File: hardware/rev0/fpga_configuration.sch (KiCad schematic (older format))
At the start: 25 parts, among them IC1 ECP5-BGA256, J5 Conn_ARM_JTAG_SWD_10, J6 Conn_ARM_JTAG_SWD_10, U6 ATSAMD21G18A-AUT, U7 W25Q32JVSS

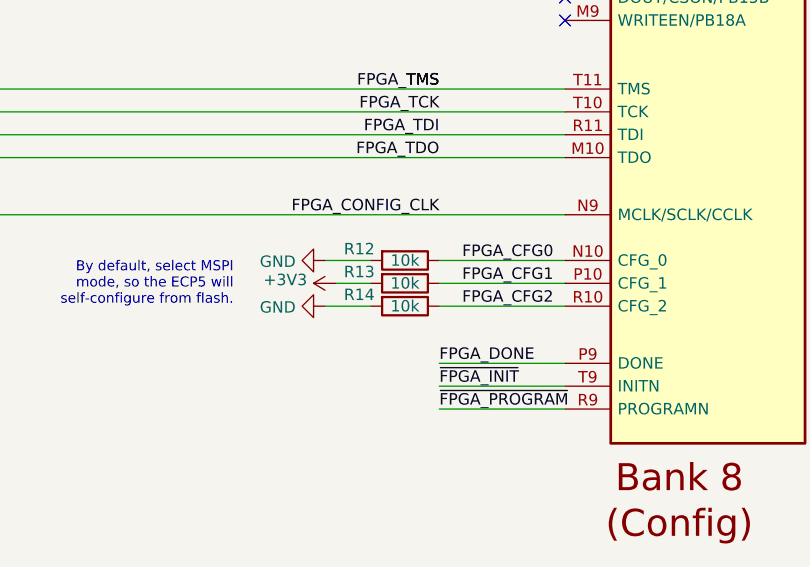
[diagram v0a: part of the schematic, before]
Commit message: hardware: add part numbers
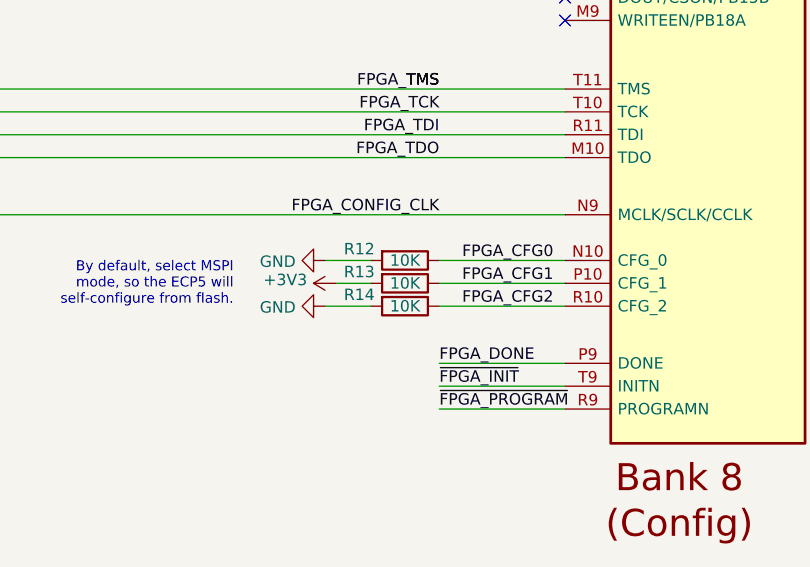
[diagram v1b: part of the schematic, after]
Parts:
- D10, D14: Manufacturer_Part_Number (none) -> GENERIC-LED-0603-BLUE
- D11, D13: Manufacturer_Part_Number (none) -> GENERIC-LED-0603-PINK
- D12: Manufacturer_Part_Number (none) -> GENERIC-LED-0603-WHITE
- J5, J6: Description (none) -> CONN HEADER VERT 10POS 1.27MM; Manufacturer_Name (none) -> Samtec; Manufacturer_Part_Number (none) -> FTSH-105-01-F-D-K
- R10, R11, R7, R8, R9: Manufacturer_Part_Number (none) -> GENERIC-RES-0402-330
- R12, R13, R14: value 10k -> 10K; Manufacturer_Part_Number (none) -> GENERIC-RES-0402-10K
- R25: Manufacturer_Part_Number (none) -> GENERIC-RES-0402-10K
- U6: Description (none) -> IC MCU 32BIT 256KB FLASH 48TQFP; Manufacturer_Name (none) -> Microchip; Manufacturer_Part_Number (none) -> ATSAMD21G18A-AUT
- U7: Description (none) -> IC FLASH 32M SPI 133MHZ 8SOIC; Manufacturer_Name (none) -> Winbond; Manufacturer_Part_Number (none) -> W25Q32JVSSIQ
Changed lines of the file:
@@
 EESchema Schematic File Version 4
-LIBS:luna_rev0-cache
 EELAYER 30 0
 EELAYER END
@@
 F 2 "Package_SO:SOIC-8_5.23x5.23mm_P1.27mm" H 7850 1350 50  0001 C CNN
 F 3 "http://www.winbond.com/resource-files/w25q32jv%20revg%2003272018%20plus.pdf" H 7850 1350 50  0001 C CNN
+F 4 "IC FLASH 32M SPI 133MHZ 8SOIC" H 7850 1350 50  0001 C CNN "Description"
+F 5 "Winbond" H 7850 1350 50  0001 C CNN "Manufacturer_Name"
+F 6 "W25Q32JVSSIQ" H 7850 1350 50  0001 C CNN "Manufacturer_Part_Number"
 	1    7850 1350
 	1    0    0    -1
@@
 P 8750 4950
 F 0 "R12" V 8700 4750 50  0000 C CNN
-F 1 "10k" V 8750 4950 50  0000 C CNN
+F 1 "10K" V 8750 4950 50  0000 C CNN
 F 2 "Resistor_SMD:R_0402_1005Metric" V 8680 4950 50  0001 C CNN
 F 3 "~" H 8750 4950 50  0001 C CNN
+F 4 "GENERIC-RES-0402-10K" H 8750 4950 50  0001 C CNN "Manufacturer_Part_Number"
 	1    8750 4950
 	0    1    1    0
@@
 P 8750 5050
 F 0 "R13" V 8700 4850 50  0000 C CNN
-F 1 "10k" V 8750 5050 50  0000 C CNN
+F 1 "10K" V 8750 5050 50  0000 C CNN
 F 2 "Resistor_SMD:R_0402_1005Metric" V 8680 5050 50  0001 C CNN
 F 3 "~" H 8750 5050 50  0001 C CNN
+F 4 "GENERIC-RES-0402-10K" H 8750 5050 50  0001 C CNN "Manufacturer_Part_Number"
 	1    8750 5050
 	0    1    1    0
@@
 P 8750 5150
 F 0 "R14" V 8700 4950 50  0000 C CNN
-F 1 "10k" V 8750 5150 50  0000 C CNN
+F 1 "10K" V 8750 5150 50  0000 C CNN
 F 2 "Resistor_SMD:R_0402_1005Metric" V 8680 5150 50  0001 C CNN
 F 3 "~" H 8750 5150 50  0001 C CNN
+F 4 "GENERIC-RES-0402-10K" H 8750 5150 50  0001 C CNN "Manufacturer_Part_Number"
 	1    8750 5150
 	0    1    1    0
@@
 F 2 "luna:SWD_CONNECTOR_LARGE_BOX" H 5850 6650 50  0001 C CNN
 F 3 "http://infocenter.arm.com/help/topic/com.arm.doc.ddi0314h/DDI0314H_coresight_components_trm.pdf" V 5500 5400 50  0001 C CNN
+F 4 "CONN HEADER VERT 10POS 1.27MM" H 5850 6650 50  0001 C CNN "Description"
+F 5 "Samtec" H 5850 6650 50  0001 C CNN "Manufacturer_Name"
+F 6 "FTSH-105-01-F-D-K" H 5850 6650 50  0001 C CNN "Manufacturer_Part_Number"
 	1    5850 6650
 	-1   0    0    -1
@@
 F 2 "LED_SMD:LED_0603_1608Metric_Pad1.05x0.95mm_HandSolder" H 4350 4050 50  0001 C CNN
 F 3 "~" H 4350 4050 50  0001 C CNN
+F 4 "GENERIC-LED-0603-PINK" H 4350 4050 50  0001 C CNN "Manufacturer_Part_Number"
 	1    4350 4050
 	1    0    0    1
@@
 F 2 "LED_SMD:LED_0603_1608Metric_Pad1.05x0.95mm_HandSolder" H 4350 4150 50  0001 C CNN
 F 3 "~" H 4350 4150 50  0001 C CNN
+F 4 "GENERIC-LED-0603-WHITE" H 4350 4150 50  0001 C CNN "Manufacturer_Part_Number"
 	1    4350 4150
 	1    0    0    1
@@
 F 2 "LED_SMD:LED_0603_1608Metric_Pad1.05x0.95mm_HandSolder" H 4350 4250 50  0001 C CNN
 F 3 "~" H 4350 4250 50  0001 C CNN
+F 4 "GENERIC-LED-0603-PINK" H 4350 4250 50  0001 C CNN "Manufacturer_Part_Number"
 	1    4350 4250
 	1    0    0    1
@@
 F 2 "LED_SMD:LED_0603_1608Metric_Pad1.05x0.95mm_HandSolder" H 4350 4350 50  0001 C CNN
 F 3 "~" H 4350 4350 50  0001 C CNN
+F 4 "GENERIC-LED-0603-BLUE" H 4350 4350 50  0001 C CNN "Manufacturer_Part_Number"
 	1    4350 4350
 	1    0    0    1
@@
 F 2 "Resistor_SMD:R_0402_1005Metric" V 3730 3950 50  0001 C CNN
 F 3 "~" H 3800 3950 50  0001 C CNN
+F 4 "GENERIC-RES-0402-330" H 3800 3950 50  0001 C CNN "Manufacturer_Part_Number"
 	1    3800 3950
 	0    1    1    0
@@
 F 2 "Resistor_SMD:R_0402_1005Metric" V 3730 4050 50  0001 C CNN
 F 3 "~" H 3800 4050 50  0001 C CNN
+F 4 "GENERIC-RES-0402-330" H 3800 4050 50  0001 C CNN "Manufacturer_Part_Number"
 	1    3800 4050
 	0    1    1    0
@@
 F 2 "Resistor_SMD:R_0402_1005Metric" V 3730 4150 50  0001 C CNN
 F 3 "~" H 3800 4150 50  0001 C CNN
+F 4 "GENERIC-RES-0402-330" H 3800 4150 50  0001 C CNN "Manufacturer_Part_Number"
 	1    3800 4150
 	0    1    1    0
@@
 F 2 "Resistor_SMD:R_0402_1005Metric" V 3730 4250 50  0001 C CNN
 F 3 "~" H 3800 4250 50  0001 C CNN
+F 4 "GENERIC-RES-0402-330" H 3800 4250 50  0001 C CNN "Manufacturer_Part_Number"
 	1    3800 4250
 	0    1    1    0
@@
 F 2 "Resistor_SMD:R_0402_1005Metric" V 3730 4350 50  0001 C CNN
 F 3 "~" H 3800 4350 50  0001 C CNN
+F 4 "GENERIC-RES-0402-330" H 3800 4350 50  0001 C CNN "Manufacturer_Part_Number"
 	1    3800 4350
 	0    1    1    0
@@
 F 2 "luna:SWD_CONNECTOR_LARGE_BOX" H 1750 6650 50  0001 C CNN
 F 3 "http://infocenter.arm.com/help/topic/com.arm.doc.ddi0314h/DDI0314H_coresight_components_trm.pdf" V 1400 5400 50  0001 C CNN
+F 4 "CONN HEADER VERT 10POS 1.27MM" H 1750 6650 50  0001 C CNN "Description"
+F 5 "Samtec" H 1750 6650 50  0001 C CNN "Manufacturer_Name"
+F 6 "FTSH-105-01-F-D-K" H 1750 6650 50  0001 C CNN "Manufacturer_Part_Number"
 	1    1750 6650
 	-1   0    0    -1
@@
 F 2 "LED_SMD:LED_0603_1608Metric_Pad1.05x0.95mm_HandSolder" H 4350 3950 50  0001 C CNN
 F 3 "~" H 4350 3950 50  0001 C CNN
+F 4 "GENERIC-LED-0603-BLUE" H 4350 3950 50  0001 C CNN "Manufacturer_Part_Number"
 	1    4350 3950
 	1    0    0    1
@@
 F 2 "Resistor_SMD:R_0402_1005Metric" V 5380 5000 50  0001 C CNN
 F 3 "~" H 5450 5000 50  0001 C CNN
+F 4 "GENERIC-RES-0402-10K" H 5450 5000 50  0001 C CNN "Manufacturer_Part_Number"
 	1    5450 5000
 	1    0    0    -1
@@
 F 2 "Package_QFP:TQFP-48_7x7mm_P0.5mm" H 1600 2000 50  0001 C CNN
 F 3 "http://ww1.microchip.com/downloads/en/DeviceDoc/SAMD21-Family-DataSheet-DS40001882D.pdf" H 2550 4750 50  0001 C CNN
+F 4 "IC MCU 32BIT 256KB FLASH 48TQFP" H 2550 3750 50  0001 C CNN "Description"
+F 5 "Microchip" H 2550 3750 50  0001 C CNN "Manufacturer_Name"
+F 6 "ATSAMD21G18A-AUT" H 2550 3750 50  0001 C CNN "Manufacturer_Part_Number"
 	1    2550 3750
 	-1   0    0    -1

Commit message: hardware: normalize BOM fields
make compatible with kicad-bom-scripts
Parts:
- C31, C32, C33, C34, C35, C51: Part Number (none) -> GENERIC-CAP-0402-0.1uF
- D10, D14: Manufacturer_Part_Number GENERIC-LED-0603-BLUE -> (none); Part Number (none) -> GENERIC-LED-0603-BLUE
- D11, D13: Manufacturer_Part_Number GENERIC-LED-0603-PINK -> (none); Part Number (none) -> GENERIC-LED-0603-PINK
- D12: Manufacturer_Part_Number GENERIC-LED-0603-WHITE -> (none); Part Number (none) -> GENERIC-LED-0603-WHITE
- IC1: Height 1.7 -> (none); Manufacturer (none) -> Lattice; Manufacturer_Name Lattice -> (none); Manufacturer_Part_Number LFE5U-12F-6BG256C -> (none); Mouser Part Number 842-LFE5U12F6BG256C -> (none); Mouser Price/Stock https://www.mouser.com/Search/Refine.aspx?Keyword=842-LFE5U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 -> (none); Part Number (none) -> LFE5U-12F-6BG256C
- J5, J6: Manufacturer (none) -> Samtec; Manufacturer_Name Samtec -> (none); Manufacturer_Part_Number FTSH-105-01-F-D-K -> (none); Part Number (none) -> FTSH-105-01-F-D-K
- R10, R11, R7, R8, R9: Manufacturer_Part_Number GENERIC-RES-0402-330 -> (none); Part Number (none) -> GENERIC-RES-0402-330
- R12, R13, R14, R25: Manufacturer_Part_Number GENERIC-RES-0402-10K -> (none); Part Number (none) -> GENERIC-RES-0402-10K
- U6: Manufacturer (none) -> Microchip; Manufacturer_Name Microchip -> (none); Manufacturer_Part_Number ATSAMD21G18A-AUT -> (none); Part Number (none) -> ATSAMD21G18A-AUT
- U7: Manufacturer (none) -> Winbond; Manufacturer_Name Winbond -> (none); Manufacturer_Part_Number W25Q32JVSSIQ -> (none); Part Number (none) -> W25Q32JVSSIQ
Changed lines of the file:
@@
 F 3 "" H 6850 6650 50  0001 L CNN
 F 4 "FPGA - Field Programmable Gate Array ECP5; 12k LUTs; 1.1V" H 6850 6550 50  0001 L CNN "Description"
-F 5 "1.7" H 6850 6900 50  0001 L CNN "Height"
-F 6 "Lattice" H 6900 7500 50  0001 L CNN "Manufacturer_Name"
-F 7 "LFE5U-12F-6BG256C" H 6900 7400 50  0001 L CNN "Manufacturer_Part_Number"
-F 8 "842-LFE5U12F6BG256C" H 7550 6100 50  0001 L CNN "Mouser Part Number"
-F 9 "https://www.mouser.com/Search/Refine.aspx?Keyword=842-LFE5U12F6BG256C" H 7200 5950 50  0001 L CNN "Mouser Price/Stock"
+F 5 "Lattice" H 6900 7500 50  0001 L CNN "Manufacturer"
+F 6 "LFE5U-12F-6BG256C" H 6900 7400 50  0001 L CNN "Part Number"
 	8    10500 2250
 	-1   0    0    -1
@@
 F 2 "Capacitor_SMD:C_0402_1005Metric" H 1438 1150 50  0001 C CNN
 F 3 "~" H 1400 1300 50  0001 C CNN
+F 4 "GENERIC-CAP-0402-0.1uF" H 1400 1300 50  0001 C CNN "Part Number"
 	1    1400 1300
 	1    0    0    -1
@@
 F 2 "Capacitor_SMD:C_0402_1005Metric" H 1738 1150 50  0001 C CNN
 F 3 "~" H 1700 1300 50  0001 C CNN
+F 4 "GENERIC-CAP-0402-0.1uF" H 1700 1300 50  0001 C CNN "Part Number"
 	1    1700 1300
 	1    0    0    -1
@@
 F 2 "Capacitor_SMD:C_0402_1005Metric" H 2038 1150 50  0001 C CNN
 F 3 "~" H 2000 1300 50  0001 C CNN
+F 4 "GENERIC-CAP-0402-0.1uF" H 2000 1300 50  0001 C CNN "Part Number"
 	1    2000 1300
 	1    0    0    -1
@@
 F 2 "Capacitor_SMD:C_0402_1005Metric" H 1138 1150 50  0001 C CNN
 F 3 "~" H 1100 1300 50  0001 C CNN
+F 4 "GENERIC-CAP-0402-0.1uF" H 1100 1300 50  0001 C CNN "Part Number"
 	1    1100 1300
 	1    0    0    -1
@@
 F 3 "http://www.winbond.com/resource-files/w25q32jv%20revg%2003272018%20plus.pdf" H 7850 1350 50  0001 C CNN
 F 4 "IC FLASH 32M SPI 133MHZ 8SOIC" H 7850 1350 50  0001 C CNN "Description"
-F 5 "Winbond" H 7850 1350 50  0001 C CNN "Manufacturer_Name"
-F 6 "W25Q32JVSSIQ" H 7850 1350 50  0001 C CNN "Manufacturer_Part_Number"
+F 5 "Winbond" H 7850 1350 50  0001 C CNN "Manufacturer"
+F 6 "W25Q32JVSSIQ" H 7850 1350 50  0001 C CNN "Part Number"
 	1    7850 1350
 	1    0    0    -1
@@
 F 2 "Capacitor_SMD:C_0402_1005Metric" H 7138 750 50  0001 C CNN
 F 3 "~" H 7100 900 50  0001 C CNN
+F 4 "GENERIC-CAP-0402-0.1uF" H 7100 900 50  0001 C CNN "Part Number"
 	1    7100 900
 	0    1    1    0
@@
 F 2 "Resistor_SMD:R_0402_1005Metric" V 8680 4950 50  0001 C CNN
 F 3 "~" H 8750 4950 50  0001 C CNN
-F 4 "GENERIC-RES-0402-10K" H 8750 4950 50  0001 C CNN "Manufacturer_Part_Number"
+F 4 "GENERIC-RES-0402-10K" H 8750 4950 50  0001 C CNN "Part Number"
 	1    8750 4950
 	0    1    1    0
@@
 F 2 "Resistor_SMD:R_0402_1005Metric" V 8680 5050 50  0001 C CNN
 F 3 "~" H 8750 5050 50  0001 C CNN
-F 4 "GENERIC-RES-0402-10K" H 8750 5050 50  0001 C CNN "Manufacturer_Part_Number"
+F 4 "GENERIC-RES-0402-10K" H 8750 5050 50  0001 C CNN "Part Number"
 	1    8750 5050
 	0    1    1    0
@@
 F 2 "Resistor_SMD:R_0402_1005Metric" V 8680 5150 50  0001 C CNN
 F 3 "~" H 8750 5150 50  0001 C CNN
-F 4 "GENERIC-RES-0402-10K" H 8750 5150 50  0001 C CNN "Manufacturer_Part_Number"
+F 4 "GENERIC-RES-0402-10K" H 8750 5150 50  0001 C CNN "Part Number"
 	1    8750 5150
 	0    1    1    0
@@
 F 3 "http://infocenter.arm.com/help/topic/com.arm.doc.ddi0314h/DDI0314H_coresight_components_trm.pdf" V 5500 5400 50  0001 C CNN
 F 4 "CONN HEADER VERT 10POS 1.27MM" H 5850 6650 50  0001 C CNN "Description"
-F 5 "Samtec" H 5850 6650 50  0001 C CNN "Manufacturer_Name"
-F 6 "FTSH-105-01-F-D-K" H 5850 6650 50  0001 C CNN "Manufacturer_Part_Number"
+F 5 "Samtec" H 5850 6650 50  0001 C CNN "Manufacturer"
+F 6 "FTSH-105-01-F-D-K" H 5850 6650 50  0001 C CNN "Part Number"
 	1    5850 6650
 	-1   0    0    -1
@@
 F 2 "LED_SMD:LED_0603_1608Metric_Pad1.05x0.95mm_HandSolder" H 4350 4050 50  0001 C CNN
 F 3 "~" H 4350 4050 50  0001 C CNN
-F 4 "GENERIC-LED-0603-PINK" H 4350 4050 50  0001 C CNN "Manufacturer_Part_Number"
+F 4 "GENERIC-LED-0603-PINK" H 4350 4050 50  0001 C CNN "Part Number"
 	1    4350 4050
 	1    0    0    1
@@
 F 2 "LED_SMD:LED_0603_1608Metric_Pad1.05x0.95mm_HandSolder" H 4350 4150 50  0001 C CNN
 F 3 "~" H 4350 4150 50  0001 C CNN
-F 4 "GENERIC-LED-0603-WHITE" H 4350 4150 50  0001 C CNN "Manufacturer_Part_Number"
+F 4 "GENERIC-LED-0603-WHITE" H 4350 4150 50  0001 C CNN "Part Number"
 	1    4350 4150
 	1    0    0    1
@@
 F 2 "LED_SMD:LED_0603_1608Metric_Pad1.05x0.95mm_HandSolder" H 4350 4250 50  0001 C CNN
 F 3 "~" H 4350 4250 50  0001 C CNN
-F 4 "GENERIC-LED-0603-PINK" H 4350 4250 50  0001 C CNN "Manufacturer_Part_Number"
+F 4 "GENERIC-LED-0603-PINK" H 4350 4250 50  0001 C CNN "Part Number"
 	1    4350 4250
 	1    0    0    1
@@
 F 2 "LED_SMD:LED_0603_1608Metric_Pad1.05x0.95mm_HandSolder" H 4350 4350 50  0001 C CNN
 F 3 "~" H 4350 4350 50  0001 C CNN
-F 4 "GENERIC-LED-0603-BLUE" H 4350 4350 50  0001 C CNN "Manufacturer_Part_Number"
+F 4 "GENERIC-LED-0603-BLUE" H 4350 4350 50  0001 C CNN "Part Number"
 	1    4350 4350
 	1    0    0    1
@@
 F 2 "Resistor_SMD:R_0402_1005Metric" V 3730 3950 50  0001 C CNN
 F 3 "~" H 3800 3950 50  0001 C CNN
-F 4 "GENERIC-RES-0402-330" H 3800 3950 50  0001 C CNN "Manufacturer_Part_Number"
+F 4 "GENERIC-RES-0402-330" H 3800 3950 50  0001 C CNN "Part Number"
 	1    3800 3950
 	0    1    1    0
@@
 F 2 "Resistor_SMD:R_0402_1005Metric" V 3730 4050 50  0001 C CNN
 F 3 "~" H 3800 4050 50  0001 C CNN
-F 4 "GENERIC-RES-0402-330" H 3800 4050 50  0001 C CNN "Manufacturer_Part_Number"
+F 4 "GENERIC-RES-0402-330" H 3800 4050 50  0001 C CNN "Part Number"
 	1    3800 4050
 	0    1    1    0
@@
 F 2 "Resistor_SMD:R_0402_1005Metric" V 3730 4150 50  0001 C CNN
 F 3 "~" H 3800 4150 50  0001 C CNN
-F 4 "GENERIC-RES-0402-330" H 3800 4150 50  0001 C CNN "Manufacturer_Part_Number"
+F 4 "GENERIC-RES-0402-330" H 3800 4150 50  0001 C CNN "Part Number"
 	1    3800 4150
 	0    1    1    0
@@
 F 2 "Resistor_SMD:R_0402_1005Metric" V 3730 4250 50  0001 C CNN
 F 3 "~" H 3800 4250 50  0001 C CNN
-F 4 "GENERIC-RES-0402-330" H 3800 4250 50  0001 C CNN "Manufacturer_Part_Number"
+F 4 "GENERIC-RES-0402-330" H 3800 4250 50  0001 C CNN "Part Number"
 	1    3800 4250
 	0    1    1    0
@@
 F 2 "Resistor_SMD:R_0402_1005Metric" V 3730 4350 50  0001 C CNN
 F 3 "~" H 3800 4350 50  0001 C CNN
-F 4 "GENERIC-RES-0402-330" H 3800 4350 50  0001 C CNN "Manufacturer_Part_Number"
+F 4 "GENERIC-RES-0402-330" H 3800 4350 50  0001 C CNN "Part Number"
 	1    3800 4350
 	0    1    1    0
@@
 F 3 "http://infocenter.arm.com/help/topic/com.arm.doc.ddi0314h/DDI0314H_coresight_components_trm.pdf" V 1400 5400 50  0001 C CNN
 F 4 "CONN HEADER VERT 10POS 1.27MM" H 1750 6650 50  0001 C CNN "Description"
-F 5 "Samtec" H 1750 6650 50  0001 C CNN "Manufacturer_Name"
-F 6 "FTSH-105-01-F-D-K" H 1750 6650 50  0001 C CNN "Manufacturer_Part_Number"
+F 5 "Samtec" H 1750 6650 50  0001 C CNN "Manufacturer"
+F 6 "FTSH-105-01-F-D-K" H 1750 6650 50  0001 C CNN "Part Number"
 	1    1750 6650
 	-1   0    0    -1
@@
 F 2 "LED_SMD:LED_0603_1608Metric_Pad1.05x0.95mm_HandSolder" H 4350 3950 50  0001 C CNN
 F 3 "~" H 4350 3950 50  0001 C CNN
-F 4 "GENERIC-LED-0603-BLUE" H 4350 3950 50  0001 C CNN "Manufacturer_Part_Number"
+F 4 "GENERIC-LED-0603-BLUE" H 4350 3950 50  0001 C CNN "Part Number"
 	1    4350 3950
 	1    0    0    1
@@
 F 2 "Resistor_SMD:R_0402_1005Metric" V 5380 5000 50  0001 C CNN
 F 3 "~" H 5450 5000 50  0001 C CNN
-F 4 "GENERIC-RES-0402-10K" H 5450 5000 50  0001 C CNN "Manufacturer_Part_Number"
+F 4 "GENERIC-RES-0402-10K" H 5450 5000 50  0001 C CNN "Part Number"
 	1    5450 5000
 	1    0    0    -1
@@
 F 2 "Capacitor_SMD:C_0402_1005Metric" H 2188 1600 50  0001 C CNN
 F 3 "~" H 2150 1750 50  0001 C CNN
+F 4 "GENERIC-CAP-0402-0.1uF" H 2150 1750 50  0001 C CNN "Part Number"
 	1    2150 1750
 	0    1    1    0
@@
 F 3 "http://ww1.microchip.com/downloads/en/DeviceDoc/SAMD21-Family-DataSheet-DS40001882D.pdf" H 2550 4750 50  0001 C CNN
 F 4 "IC MCU 32BIT 256KB FLASH 48TQFP" H 2550 3750 50  0001 C CNN "Description"
-F 5 "Microchip" H 2550 3750 50  0001 C CNN "Manufacturer_Name"
-F 6 "ATSAMD21G18A-AUT" H 2550 3750 50  0001 C CNN "Manufacturer_Part_Number"
+F 5 "Microchip" H 2550 3750 50  0001 C CNN "Manufacturer"
+F 6 "ATSAMD21G18A-AUT" H 2550 3750 50  0001 C CNN "Part Number"
 	1    2550 3750
 	-1   0    0    -1
